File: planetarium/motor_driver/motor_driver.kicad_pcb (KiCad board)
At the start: 2 copper layers, 77.5 x 48 mm, 20 parts, among them J1 Jack-DC, J2 Conn_01x05, Q1 Q_PMOS, SW1 1k, U1 SLA7078MPRT, U2 XIAO-ESP32-C3-SMD, U3 BP5293-50

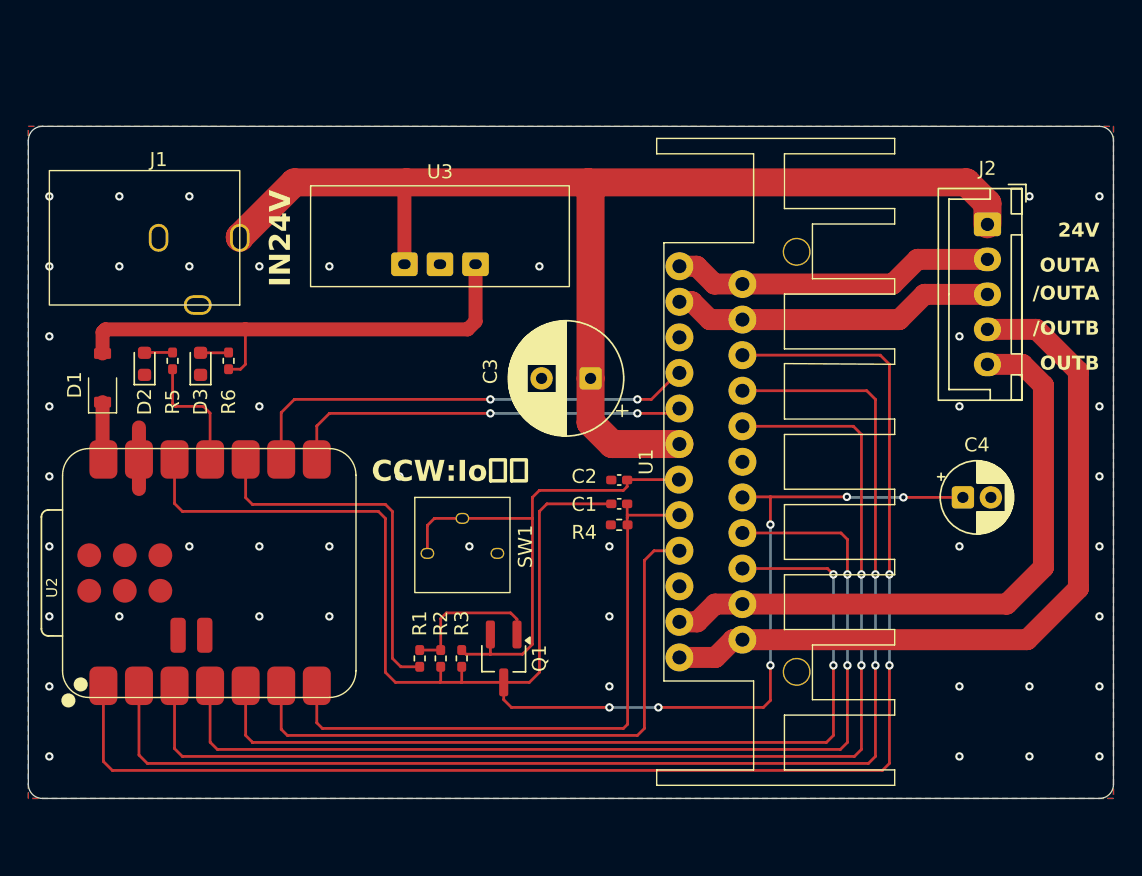
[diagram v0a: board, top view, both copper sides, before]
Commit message: fix:PMOSのDとS間違えてた
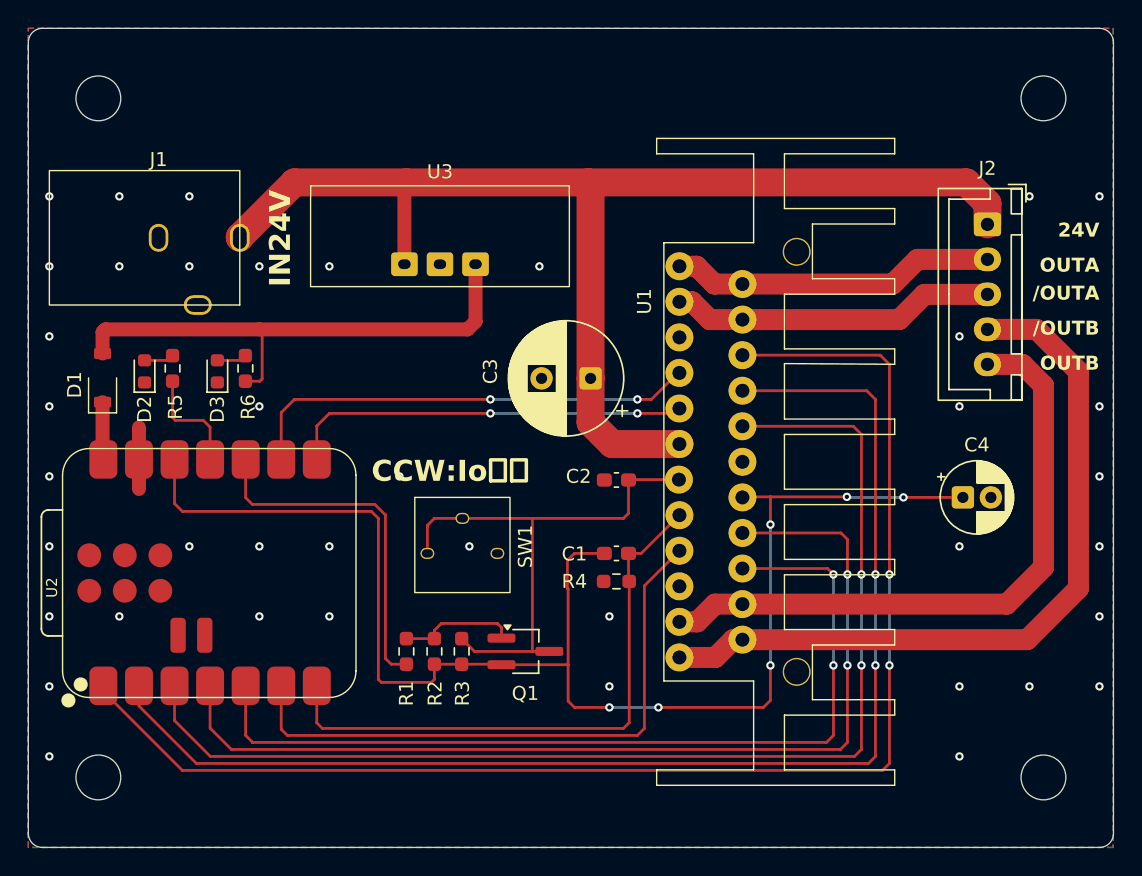
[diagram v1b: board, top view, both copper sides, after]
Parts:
- added REF**: MountingHole_3.2mm_M3, MountingHole:MountingHole_3.2mm_M3, F.Cu at (146.0, 121.5)
- added REF**: MountingHole_3.2mm_M3, MountingHole:MountingHole_3.2mm_M3, F.Cu at (78.5, 73.0)
- added REF**: MountingHole_3.2mm_M3, MountingHole:MountingHole_3.2mm_M3, F.Cu at (78.5, 121.5)
- added REF**: MountingHole_3.2mm_M3, MountingHole:MountingHole_3.2mm_M3, F.Cu at (146.0, 73.0)
- C1, C2: footprint Capacitor_SMD:C_0402_1005Metric_Pad0.74x0.62mm_HandSolder -> Capacitor_SMD:C_0603_1608Metric_Pad1.08x0.95mm_HandSolder
- R1, R2, R3, R4, R5, R6: footprint Resistor_SMD:R_0402_1005Metric_Pad0.72x0.64mm_HandSolder -> Resistor_SMD:R_0603_1608Metric_Pad0.98x0.95mm_HandSolder
- moved R4 4.04 mm to (115.5, 107.5)
- moved C1 3.55 mm to (115.5, 105.5)
- moved Q1 1.63 mm to (109.0, 112.5), turned to 0 degrees
- moved D3 1.32 mm to (87.0, 92.5)
- moved R6 1.32 mm to (89.0, 92.3)
- moved R1 1.07 mm to (100.5, 112.5)
- moved R2 0.67 mm to (102.5, 112.5)
- moved D2 0.54 mm to (81.8, 92.5)
- moved R5 0.54 mm to (83.8, 92.3)
- moved R3 0.50 mm to (104.5, 112.5)
- moved C2 0.20 mm to (115.5, 100.3)
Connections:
- Q1 pad D: +3.3V -> /ref/sleep_driver
- Q1 pad S: /ref/sleep_driver -> +3.3V
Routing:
- net +3.3V: track 111.4 -> 102.6 mm
- net /Mo: track 101.3 -> 98.4 mm
- net /reset: track 44.6 -> 42.2 mm
- net Net-(Q1-PadG): track 10.6 -> 8.46 mm
- net /M2: track 93.3 -> 91.2 mm
- net /clk: track 85.2 -> 84.1 mm
- net /ref/sleep_mcu: track 26.3 -> 25.1 mm
- net /sync: track 44.2 -> 43.2 mm
- net +5V: track 36.4 -> 37.5 mm
- net /led_status: track 8.73 -> 7.87 mm
- net /cw/ccw: track 72.2 -> 71.6 mm
- net GND: vias 43 -> 40
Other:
- board size 77.5 x 48 mm -> 77.5 x 58.5 mm
